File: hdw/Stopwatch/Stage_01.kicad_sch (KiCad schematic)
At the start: 5 parts, among them U901 4026, U902 HDSP-7503

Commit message: started sch work
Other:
- moved on the sheet: C901

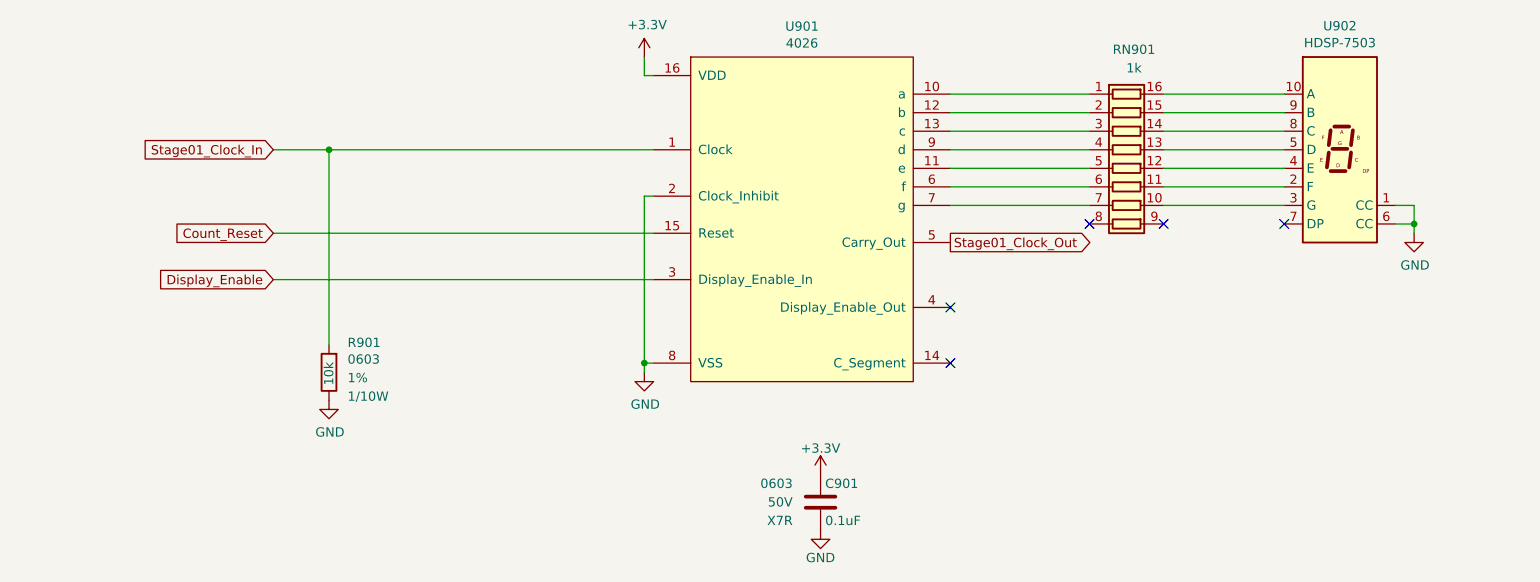
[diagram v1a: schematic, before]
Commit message: adjusted stage sheet
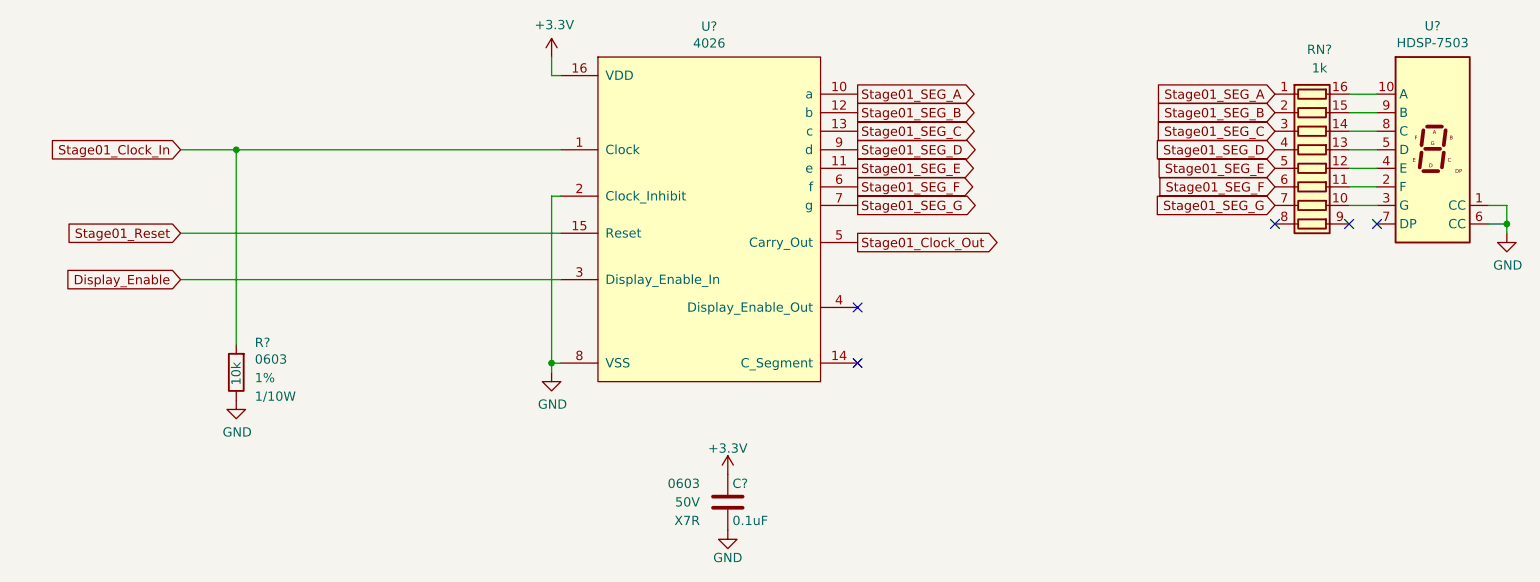
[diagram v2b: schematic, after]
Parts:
- renumbered C901 to C?, R901 to R?, RN901 to RN?, U901 to U?, U902 to U?
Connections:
- net Stage01_SEG_A: now reaches RN?.1 (R1.1), U?.10 (a)
- net Stage01_SEG_E: now reaches RN?.5 (R5.1), U?.11 (e)
- net Stage01_SEG_B: now reaches RN?.2 (R2.1), U?.12 (b)
- net Stage01_SEG_C: now reaches RN?.3 (R3.1), U?.13 (c)
- net Stage01_SEG_F: now reaches RN?.6 (R6.1), U?.6 (f)
- net Stage01_SEG_G: now reaches RN?.7 (R7.1), U?.7 (g)
- net Stage01_SEG_D: now reaches RN?.4 (R4.1), U?.9 (d)
- net Count_Reset renamed Stage01_Reset
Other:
- moved on the sheet: C?, R?, RN?, U?

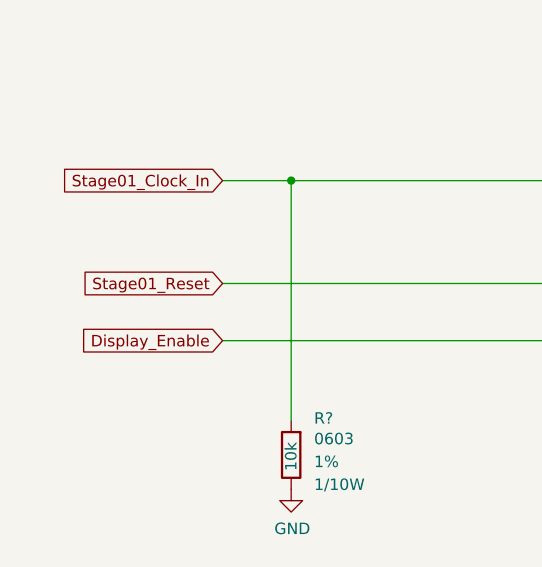
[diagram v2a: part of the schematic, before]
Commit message: copied to minutes reset sheet
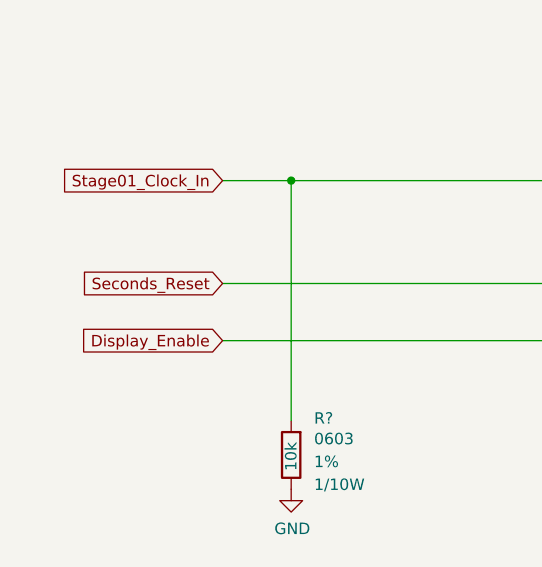
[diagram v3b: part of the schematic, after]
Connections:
- net Stage01_Reset renamed Seconds_Reset
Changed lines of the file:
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@@
-    )
-  )
-  (global_label "Stage01_Reset" (shape input) (at 55.88 92.71 180)
-    (effects (font (size 1.27 1.27)) (justify right))
-    (property "Intersheetrefs" "${INTERSHEET_REFS}" (at 55.88 92.71 0)
-      (effects (font (size 1.27 1.27)) hide)
     )
   )
@@
     )
   )
+  (global_label "Seconds_Reset" (shape input) (at 55.88 92.71 180) (fields_autoplaced)
+    (effects (font (size 1.27 1.27)) (justify right))
+    (property "Intersheetrefs" "${INTERSHEET_REFS}" (at 39.598 92.71 0)
+      (effects (font (size 1.27 1.27)) (justify right) hide)
+    )
+  )

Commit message: added some more junk
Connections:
- net Stage01_Clock_In renamed 1Hz_Clock
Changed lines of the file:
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@@
   (title_block
     (title "Stopwatch")
-    (date "2024-01-02")
+    (date "2024-01-11")
     (rev "A")
     (company "Drew Maatman")
@@
     )
   )
-  (global_label "Stage01_Clock_In" (shape input) (at 55.88 81.28 180)
+  (global_label "1Hz_Clock" (shape input) (at 55.88 81.28 180)
     (effects (font (size 1.27 1.27)) (justify right))
     (property "Intersheetrefs" "${INTERSHEET_REFS}" (at 55.88 81.28 0)

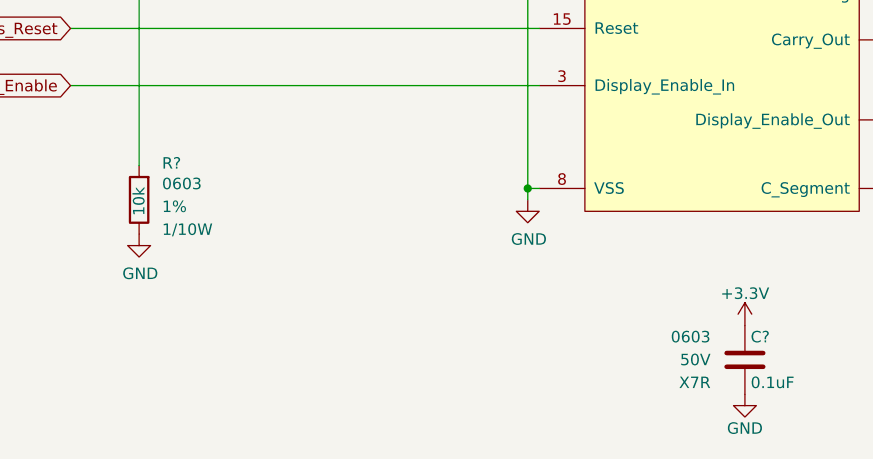
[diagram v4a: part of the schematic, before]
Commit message: Assigned some digikey pns
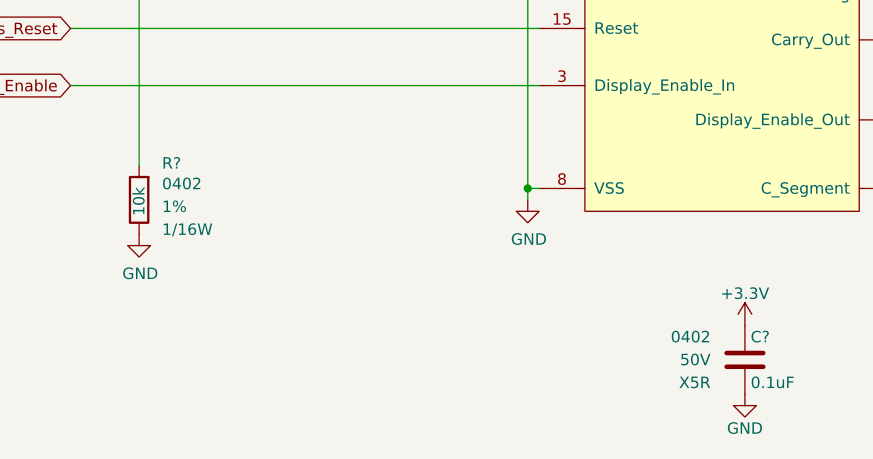
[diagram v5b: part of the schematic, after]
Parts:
- C?: footprint Capacitors_SMD:C_0603 -> Capacitors_SMD:C_0402; Dielectric X7R -> X5R; Digi-Key PN 311-1344-1-ND -> 490-10697-1-ND; display_footprint 0603 -> 0402
- R?: footprint Resistors_SMD:R_0603 -> Resistors_SMD:R_0402; Digi-Key PN RMCF0603FT10K0CT-ND -> RMCF0402FT10K0CT-ND; Wattage 1/10W -> 1/16W; display_footprint 0603 -> 0402
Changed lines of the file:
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@@
       (effects (font (size 1.27 1.27)) (justify left))
     )
-    (property "Footprint" "Resistors_SMD:R_0603" (at 63.5 111.76 0)
+    (property "Footprint" "Resistors_SMD:R_0402" (at 63.5 111.76 0)
       (effects (font (size 1.27 1.27)) hide)
     )
@@
       (effects (font (size 1.27 1.27)) hide)
     )
-    (property "display_footprint" "0603" (at 66.04 109.982 0)
+    (property "display_footprint" "0402" (at 66.04 109.982 0)
       (effects (font (size 1.27 1.27)) (justify left))
     )
@@
       (effects (font (size 1.27 1.27)) (justify left))
     )
-    (property "Wattage" "1/10W" (at 66.04 115.062 0)
+    (property "Wattage" "1/16W" (at 66.04 115.062 0)
       (effects (font (size 1.27 1.27)) (justify left))
     )
-    (property "Digi-Key PN" "RMCF0603FT10K0CT-ND" (at 71.12 101.6 0)
+    (property "Digi-Key PN" "RMCF0402FT10K0CT-ND" (at 71.12 101.6 0)
       (effects (font (size 1.524 1.524)) hide)
     )
@@
       (effects (font (size 1.27 1.27)) (justify left))
     )
-    (property "Footprint" "Capacitors_SMD:C_0603" (at 131.7752 133.35 0)
+    (property "Footprint" "Capacitors_SMD:C_0402" (at 131.7752 133.35 0)
       (effects (font (size 1.27 1.27)) hide)
     )
@@
       (effects (font (size 1.27 1.27)) hide)
     )
-    (property "display_footprint" "0603" (at 127 127 0)
+    (property "display_footprint" "0402" (at 127 127 0)
       (effects (font (size 1.27 1.27)) (justify right))
     )
@@
       (effects (font (size 1.27 1.27)) (justify right))
     )
-    (property "Dielectric" "X7R" (at 127 132.08 0)
+    (property "Dielectric" "X5R" (at 127 132.08 0)
       (effects (font (size 1.27 1.27)) (justify right))
     )
-    (property "Digi-Key PN" "311-1344-1-ND" (at 141.605 116.84 0)
+    (property "Digi-Key PN" "490-10697-1-ND" (at 141.605 116.84 0)
       (effects (font (size 1.524 1.524)) hide)
     )

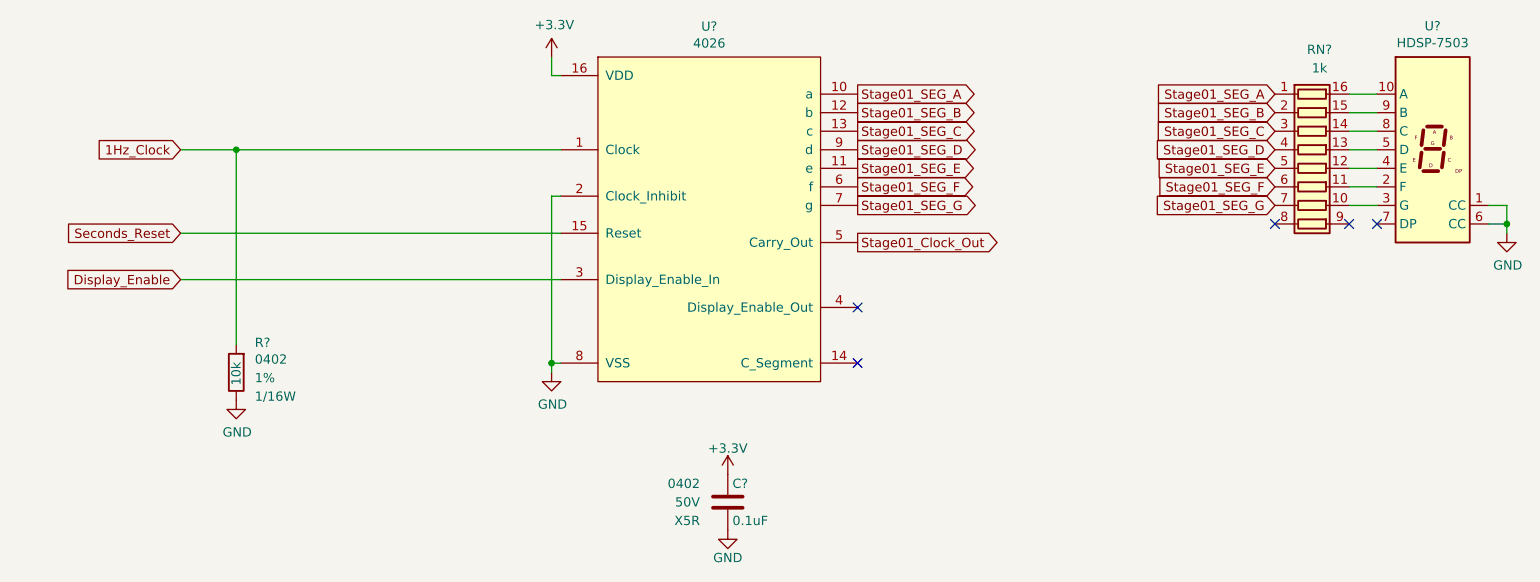
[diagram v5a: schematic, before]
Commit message: added proper power sequencing, discharge
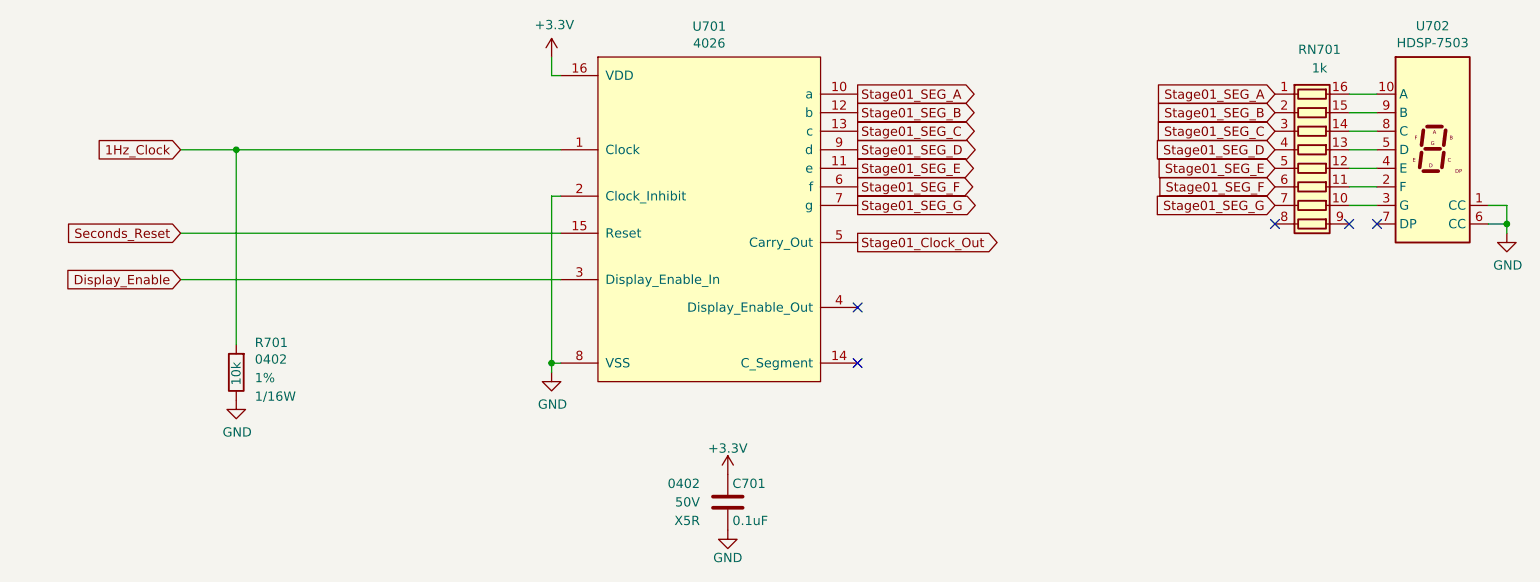
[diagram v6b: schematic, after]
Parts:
- gave numbers to parts that had none: 5
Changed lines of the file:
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@@
   (symbol (lib_id "Custom_Library:4026") (at 107.95 71.12 0) (unit 1)
     (in_bom yes) (on_board yes) (dnp no)
-    (property "Reference" "U?" (at 128.27 64.389 0)
+    (property "Reference" "U701" (at 128.27 64.389 0)
       (effects (font (size 1.27 1.27)))
     )
@@
       (project "Stopwatch"
         (path "/c0d2575b-aec2-49ed-8c32-97fe6e68824c/00000000-0000-0000-0000-00005d6b2673"
-          (reference "U?") (unit 1)
+          (reference "U701") (unit 1)
         )
       )
@@
   (symbol (lib_id "Incrementor-rescue:+3.3V-power") (at 106.68 68.58 0) (unit 1)
     (in_bom yes) (on_board yes) (dnp no)
-    (property "Reference" "#PWR?" (at 106.68 72.39 0)
+    (property "Reference" "#PWR0702" (at 106.68 72.39 0)
       (effects (font (size 1.27 1.27)) hide)
     )
@@
       (project "Stopwatch"
         (path "/c0d2575b-aec2-49ed-8c32-97fe6e68824c/00000000-0000-0000-0000-00005d6b2673"
-          (reference "#PWR?") (unit 1)
+          (reference "#PWR0702") (unit 1)
         )
       )
@@
   (symbol (lib_id "power:GND") (at 106.68 111.76 0) (unit 1)
     (in_bom yes) (on_board yes) (dnp no)
-    (property "Reference" "#PWR?" (at 106.68 118.11 0)
+    (property "Reference" "#PWR0703" (at 106.68 118.11 0)
       (effects (font (size 1.27 1.27)) hide)
     )
@@
       (project "Stopwatch"
         (path "/c0d2575b-aec2-49ed-8c32-97fe6e68824c/00000000-0000-0000-0000-00005d6b2673"
-          (reference "#PWR?") (unit 1)
+          (reference "#PWR0703") (unit 1)
         )
       )
@@
   (symbol (lib_id "Device:R_Pack08") (at 210.82 83.82 270) (unit 1)
     (in_bom yes) (on_board yes) (dnp no)
-    (property "Reference" "RN?" (at 211.836 67.564 90)
+    (property "Reference" "RN701" (at 211.836 67.564 90)
       (effects (font (size 1.27 1.27)))
     )
@@
       (project "Stopwatch"
         (path "/c0d2575b-aec2-49ed-8c32-97fe6e68824c/00000000-0000-0000-0000-00005d6b2673"
-          (reference "RN?") (unit 1)
+          (reference "RN701") (unit 1)
         )
       )
@@
   (symbol (lib_id "Display_Character:HDSP-7503") (at 227.33 81.28 0) (unit 1)
     (in_bom yes) (on_board yes) (dnp no)
-    (property "Reference" "U?" (at 227.33 64.3382 0)
+    (property "Reference" "U702" (at 227.33 64.3382 0)
       (effects (font (size 1.27 1.27)))
     )
@@
       (project "Stopwatch"
         (path "/c0d2575b-aec2-49ed-8c32-97fe6e68824c/00000000-0000-0000-0000-00005d6b2673"
-          (reference "U?") (unit 1)
+          (reference "U702") (unit 1)
         )
       )
@@
   (symbol (lib_id "power:GND") (at 237.49 92.71 0) (unit 1)
     (in_bom yes) (on_board yes) (dnp no)
-    (property "Reference" "#PWR?" (at 237.49 99.06 0)
+    (property "Reference" "#PWR0706" (at 237.49 99.06 0)
       (effects (font (size 1.27 1.27)) hide)
     )
@@
       (project "Stopwatch"
         (path "/c0d2575b-aec2-49ed-8c32-97fe6e68824c/00000000-0000-0000-0000-00005d6b2673"
-          (reference "#PWR?") (unit 1)
+          (reference "#PWR0706") (unit 1)
         )
       )
@@
   (symbol (lib_id "Custom_Library:R_Custom") (at 63.5 111.76 0) (unit 1)
     (in_bom yes) (on_board yes) (dnp no)
-    (property "Reference" "R?" (at 66.04 107.696 0)
+    (property "Reference" "R701" (at 66.04 107.696 0)
       (effects (font (size 1.27 1.27)) (justify left))
     )
@@
       (project "Stopwatch"
         (path "/c0d2575b-aec2-49ed-8c32-97fe6e68824c/00000000-0000-0000-0000-00005d6b2673"
-          (reference "R?") (unit 1)
+          (reference "R701") (unit 1)
         )
       )
@@
   (symbol (lib_id "power:GND") (at 63.5 115.57 0) (unit 1)
     (in_bom yes) (on_board yes) (dnp no)
-    (property "Reference" "#PWR?" (at 63.5 121.92 0)
+    (property "Reference" "#PWR0701" (at 63.5 121.92 0)
       (effects (font (size 1.27 1.27)) hide)
     )
@@
       (project "Stopwatch"
         (path "/c0d2575b-aec2-49ed-8c32-97fe6e68824c/00000000-0000-0000-0000-00005d6b2673"
-          (reference "#PWR?") (unit 1)
+          (reference "#PWR0701") (unit 1)
         )
       )
@@
   (symbol (lib_id "Custom_Library:C_Custom") (at 130.81 129.54 0) (unit 1)
     (in_bom yes) (on_board yes) (dnp no)
-    (property "Reference" "C?" (at 131.445 127 0)
+    (property "Reference" "C701" (at 131.445 127 0)
       (effects (font (size 1.27 1.27)) (justify left))
     )
@@
       (project "Stopwatch"
         (path "/c0d2575b-aec2-49ed-8c32-97fe6e68824c/00000000-0000-0000-0000-00005d6b2673"
-          (reference "C?") (unit 1)
+          (reference "C701") (unit 1)
         )
       )
@@
   (symbol (lib_id "power:GND") (at 130.81 133.35 0) (unit 1)
     (in_bom yes) (on_board yes) (dnp no)
-    (property "Reference" "#PWR?" (at 130.81 139.7 0)
+    (property "Reference" "#PWR0705" (at 130.81 139.7 0)
       (effects (font (size 1.27 1.27)) hide)
     )
@@
       (project "Stopwatch"
         (path "/c0d2575b-aec2-49ed-8c32-97fe6e68824c/00000000-0000-0000-0000-00005d6b2673"
-          (reference "#PWR?") (unit 1)
+          (reference "#PWR0705") (unit 1)
         )
       )
@@
   (symbol (lib_id "Incrementor-rescue:+3.3V-power") (at 130.81 125.73 0) (unit 1)
     (in_bom yes) (on_board yes) (dnp no)
-    (property "Reference" "#PWR?" (at 130.81 129.54 0)
+    (property "Reference" "#PWR0704" (at 130.81 129.54 0)
       (effects (font (size 1.27 1.27)) hide)
     )
@@
       (project "Stopwatch"
         (path "/c0d2575b-aec2-49ed-8c32-97fe6e68824c/00000000-0000-0000-0000-00005d6b2673"
-          (reference "#PWR?") (unit 1)
-        )
-      )
+          (reference "#PWR0704") (unit 1)
+        )
+      )

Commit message: lots and lots of routing
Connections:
- net +3V3 renamed +3.3V
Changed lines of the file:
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@@
     )
   )
-  (symbol (lib_id "Incrementor-rescue:+3.3V-power") (at 106.68 68.58 0) (unit 1)
+  (symbol (lib_id "power:+3.3V") (at 106.68 68.58 0) (unit 1)
     (in_bom yes) (on_board yes) (dnp no)
     (property "Reference" "#PWR0702" (at 106.68 72.39 0)
@@
     )
   )
-  (symbol (lib_id "Incrementor-rescue:+3.3V-power") (at 130.81 125.73 0) (unit 1)
+  (symbol (lib_id "power:+3.3V") (at 130.81 125.73 0) (unit 1)
     (in_bom yes) (on_board yes) (dnp no)
     (property "Reference" "#PWR0704" (at 130.81 129.54 0)
